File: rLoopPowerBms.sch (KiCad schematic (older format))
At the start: 66 parts, among them P1 CONN_01X07, P2 EXT-TMP, Q1 BSS138, Q2 BSS138, Q3 BSS138, Q4 BSS138, Q5 BSS138, Q6 BSS138, U1 ATA6870N_BMS

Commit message: rdy for review, added req'ed bits for top board
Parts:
- added C11, C12: 100nF, Capacitors_SMD:C_0603, symbol Cap
- added D7: 8V Zener, Diodes_SMD:SOD-123, symbol ZENERsmall
- added JP2, JP3: Jumper_NC_Small, Connect:GS2, symbol Jumper_NC_Small
- added Q7: Q_PMOS, TO_SOT_Packages_SMD:SOT-23, symbol Q_PMOS_GSD
- added R14, R15, R17: 10KΩ, Resistors_SMD:R_0603, symbol R-RESCUE-rLoopPowerBms
- added R16: 150Ω, Resistors_SMD:R_0603, symbol R-RESCUE-rLoopPowerBms
- added R18: 10K, symbol R
- added U2: D_Flip_Flop_w_Inv_Out, TO_SOT_Packages_SMD:SOT-23-5, symbol D_Flip_Flop_w_Inv_Out
- added U3: 1MHz Oscillator, -footprints:Oscillator_SMD_4_pin_2.5x2mm, symbol Oscillator_SMD_4_pin
- added X1: AMPMODU-02X05, -footprints:AMPMODU-02X05-0.05in-MECHHOLES, symbol AMPMODU-02X05
- added X2: AMPMODU-02X05, -footprints:AMPMODU-02X05-0.05in-NOHOLES, symbol AMPMODU-02X05
- C10: value 33uF PolC -> 33uF
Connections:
- net labels added: CLK, CLK-HIGHER, CS-HIGHER, CS-LOWER, IRQ-HIGHER, IRQ-LOWER, MISO-HIGHER, MISO-LOWER, MOSI-HIGHER, MOSI-LOWER, PD-HIGHER, PD-LOWER, PD-MASTER, SCK-HIGHER, SCK-LOWER, VDD, VDD-HIGHER
- wire segments 300 -> 347
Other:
- note added: "Required only for top board"
- note added: "generates a 500KHz clock\nonly the bottom board need a clock source"
- note removed: "To higher board / terminator"
- note removed: "To lower board / master"
- moved on the sheet: C10, C7, C8

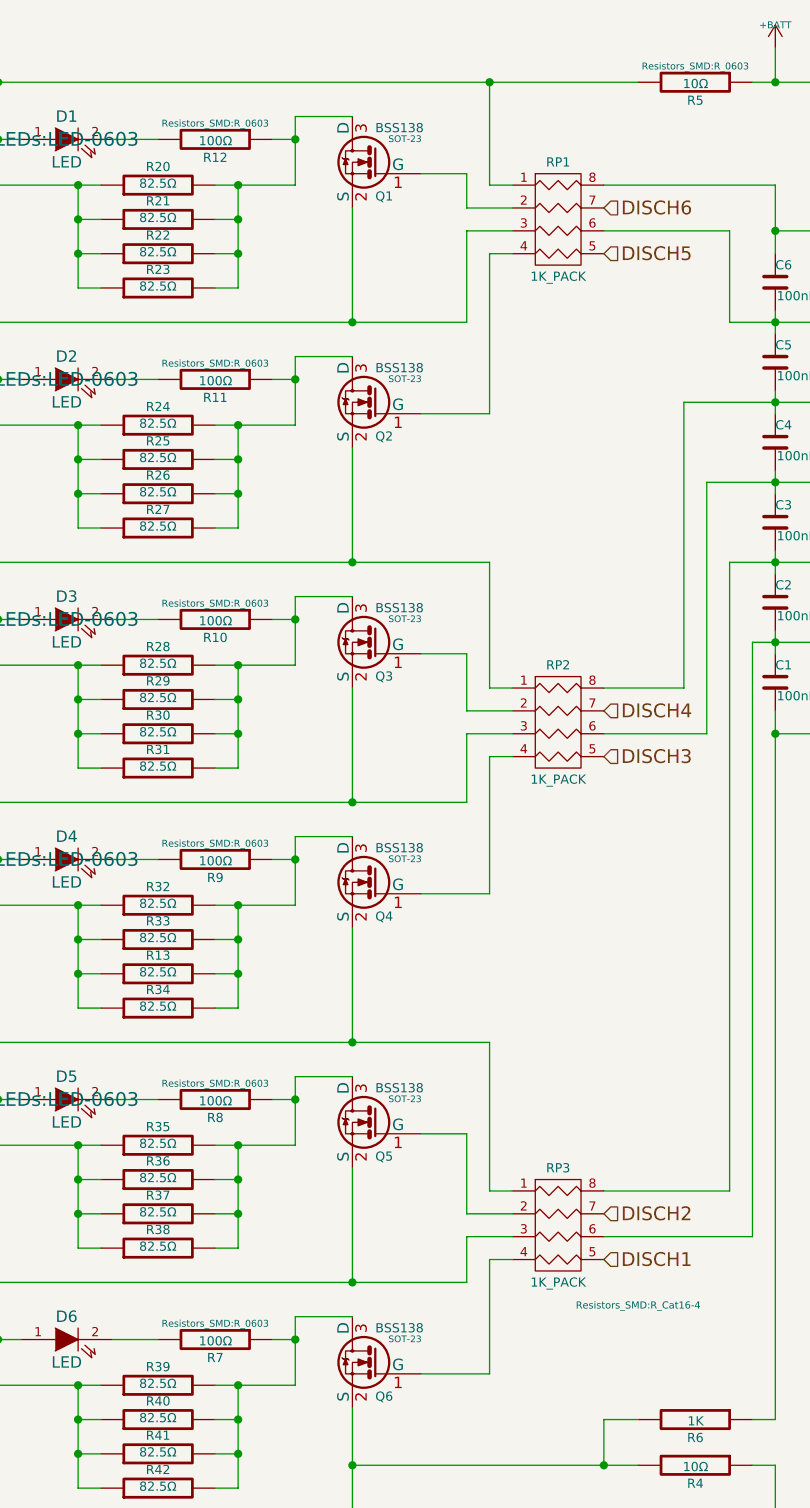
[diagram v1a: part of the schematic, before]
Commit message: missed R18
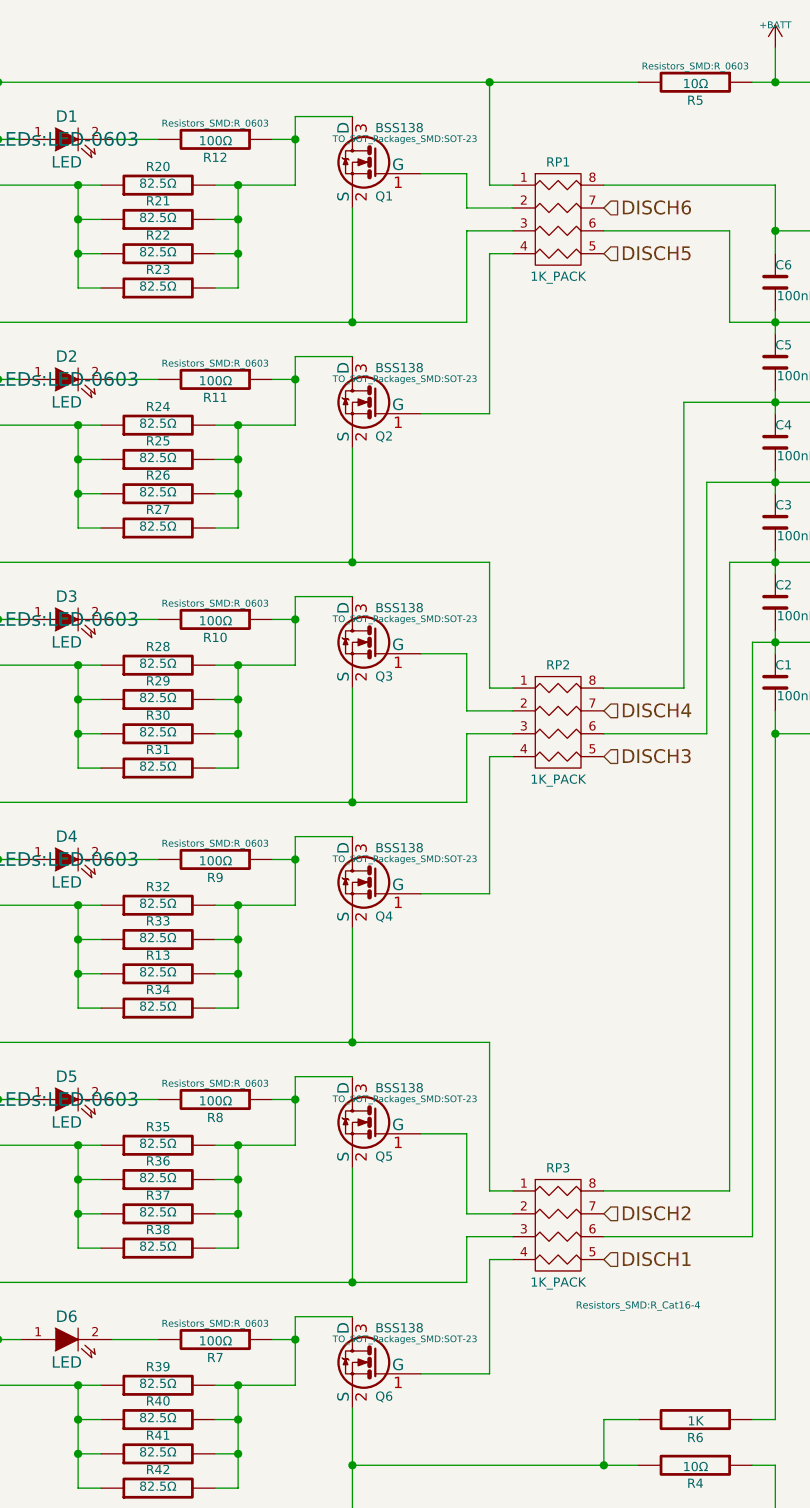
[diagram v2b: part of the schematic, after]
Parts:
- Q1, Q2, Q3, Q4, Q5, Q6: footprint SOT-23 -> TO_SOT_Packages_SMD:SOT-23
- R18, R6: footprint (none) -> Resistors_SMD:R_0603
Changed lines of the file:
@@
 F 0 "Q1" H 3650 1451 40  0000 R CNN
 F 1 "BSS138" H 3650 1750 40  0000 R CNN
-F 2 "SOT-23" H 3520 1702 29  0000 C CNN
+F 2 "TO_SOT_Packages_SMD:SOT-23" H 3520 1702 29  0000 C CNN
 F 3 "~" H 3650 1600 60  0000 C CNN
 	1    3650 1600
@@
 F 0 "Q2" H 3650 2501 40  0000 R CNN
 F 1 "BSS138" H 3650 2800 40  0000 R CNN
-F 2 "SOT-23" H 3520 2752 29  0000 C CNN
+F 2 "TO_SOT_Packages_SMD:SOT-23" H 3520 2752 29  0000 C CNN
 F 3 "~" H 3650 2650 60  0000 C CNN
 	1    3650 2650
@@
 F 0 "Q3" H 3650 3551 40  0000 R CNN
 F 1 "BSS138" H 3650 3850 40  0000 R CNN
-F 2 "SOT-23" H 3520 3802 29  0000 C CNN
+F 2 "TO_SOT_Packages_SMD:SOT-23" H 3520 3802 29  0000 C CNN
 F 3 "~" H 3650 3700 60  0000 C CNN
 	1    3650 3700
@@
 F 0 "Q6" H 3650 6701 40  0000 R CNN
 F 1 "BSS138" H 3650 7000 40  0000 R CNN
-F 2 "SOT-23" H 3520 6952 29  0000 C CNN
+F 2 "TO_SOT_Packages_SMD:SOT-23" H 3520 6952 29  0000 C CNN
 F 3 "~" H 3650 6850 60  0000 C CNN
 	1    3650 6850
@@
 F 0 "Q4" H 3650 4601 40  0000 R CNN
 F 1 "BSS138" H 3650 4900 40  0000 R CNN
-F 2 "SOT-23" H 3520 4852 29  0000 C CNN
+F 2 "TO_SOT_Packages_SMD:SOT-23" H 3520 4852 29  0000 C CNN
 F 3 "~" H 3650 4750 60  0000 C CNN
 	1    3650 4750
@@
 F 0 "Q5" H 3650 5651 40  0000 R CNN
 F 1 "BSS138" H 3650 5950 40  0000 R CNN
-F 2 "SOT-23" H 3520 5902 29  0000 C CNN
+F 2 "TO_SOT_Packages_SMD:SOT-23" H 3520 5902 29  0000 C CNN
 F 3 "~" H 3650 5800 60  0000 C CNN
 	1    3650 5800
@@
 F 0 "R6" V 5130 7100 40  0000 C CNN
 F 1 "1K" V 5057 7101 40  0000 C CNN
-F 2 "" V 4980 7100 30  0000 C CNN
+F 2 "Resistors_SMD:R_0603" V 4980 7100 30  0001 C CNN
 F 3 "" H 5050 7100 30  0000 C CNN
 	1    5050 7100
@@
 F 0 "R18" V 9580 4150 50  0000 C CNN
 F 1 "10K" V 9500 4150 50  0000 C CNN
-F 2 "" V 9430 4150 50  0000 C CNN
+F 2 "Resistors_SMD:R_0603" V 9430 4150 50  0001 C CNN
 F 3 "" H 9500 4150 50  0000 C CNN
 	1    9500 4150
